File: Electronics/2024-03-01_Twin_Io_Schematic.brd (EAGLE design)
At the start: 160 x 100 mm, 179 parts, among them IC1 7805, IC2 LD1117S33, J1 12402012E212A, U1 INA317IDGKT, U10 INA317IDGKT, U11 INA317IDGKT, U12 INA317IDGKT, U13 ADS131A04IPBSR, U14 ADS131A04IPBSR, U15 ADS131A04IPBSR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

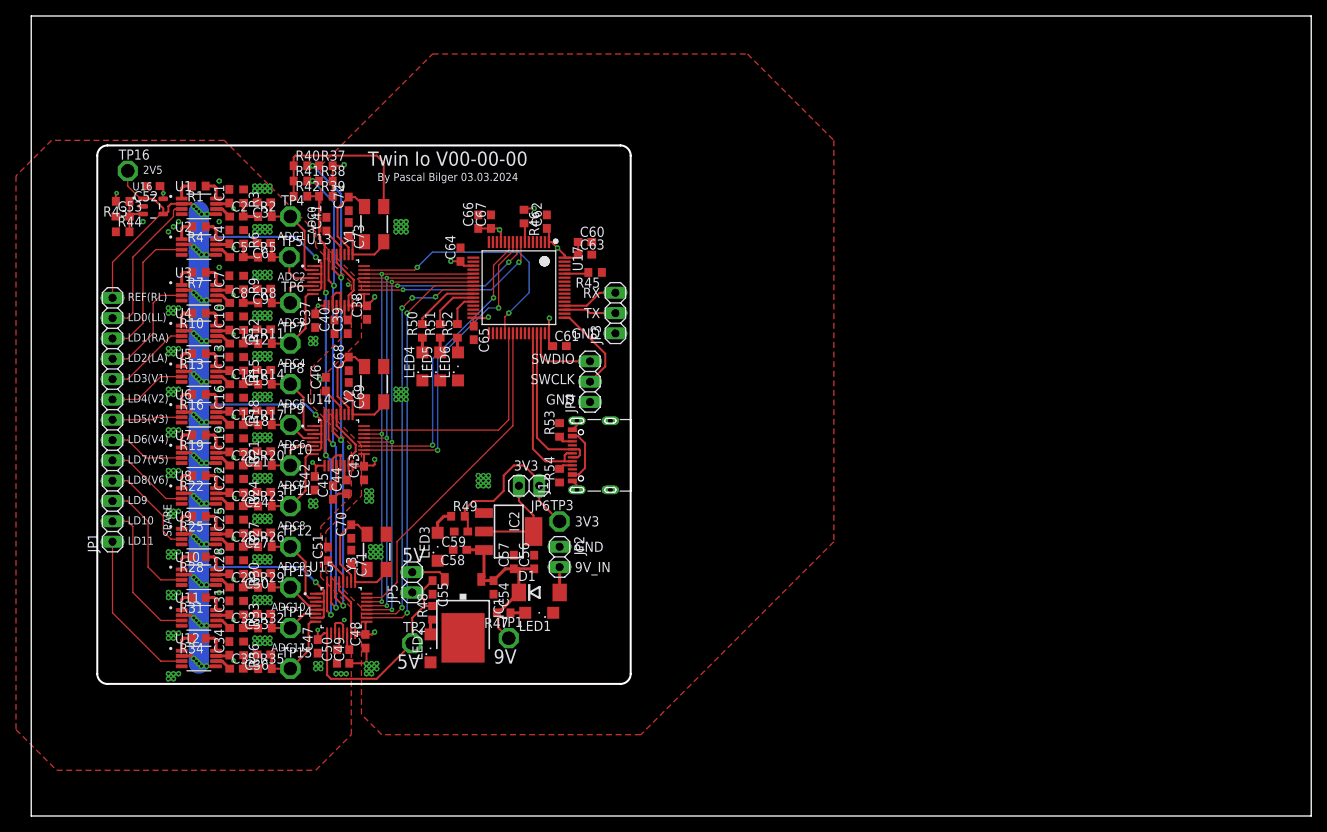
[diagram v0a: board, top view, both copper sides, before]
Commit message: Added possibility for STM32 Timer output to be used for the ADC clock, selectable by 3x 0Ohm resistors
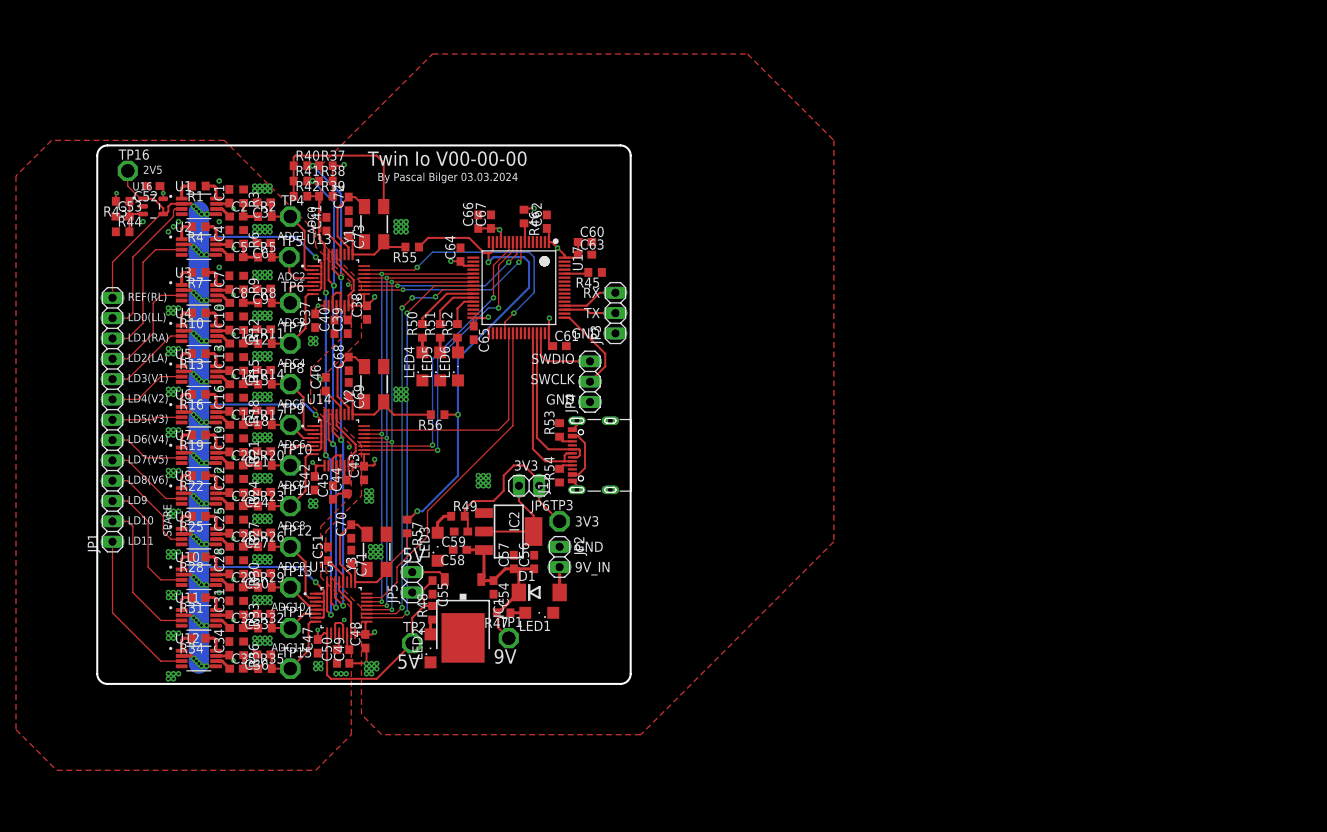
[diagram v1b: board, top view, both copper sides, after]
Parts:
- added R55, R56, R57: 0R, rcl:R0603
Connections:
- new net ADC_CLK: R55.1, R56.1, R57.1, U17.15
- net N$43: now also R56.2
- net N$51: now also R57.2
- net N$8: now also R55.2
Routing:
- net ADC_CLK: track 0.00 -> 59.1 mm, vias 0 -> 3
- net N$43: track 7.30 -> 13.7 mm
- net N$51: track 7.30 -> 12.9 mm
- net N$8: track 7.30 -> 10.3 mm
- net ADC0_CS: track 32.2 -> 33.5 mm
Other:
- board size 160 x 100 mm -> 66.7 x 67.3 mm
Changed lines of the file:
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@@
 <layer number="14" name="Route14" color="22" fill="1" visible="no" active="no"/>
 <layer number="15" name="Route15" color="23" fill="1" visible="no" active="yes"/>
-<layer number="16" name="Bottom" color="1" fill="1" visible="no" active="yes"/>
+<layer number="16" name="Bottom" color="1" fill="1" visible="yes" active="yes"/>
 <layer number="17" name="Pads" color="2" fill="1" visible="yes" active="yes"/>
 <layer number="18" name="Vias" color="2" fill="1" visible="yes" active="yes"/>
@@
 <board>
 <plain>
-<wire x1="0" y1="0" x2="160" y2="0" width="0" layer="20"/>
-<wire x1="160" y1="0" x2="160" y2="100" width="0" layer="20"/>
-<wire x1="160" y1="100" x2="0" y2="100" width="0" layer="20"/>
-<wire x1="0" y1="100" x2="0" y2="0" width="0" layer="20"/>
 <text x="57.785" y="19.05" size="1.778" layer="21">9V</text>
 <text x="45.72" y="18.415" size="1.778" layer="21">5V</text>
@@
 <attribute name="VALUE" x="64.77" y="44.45" size="1.27" layer="27" rot="R180"/>
 </element>
+<element name="R55" library="rcl" library_urn="urn:adsk.eagle:library:334" package="R0603" package3d_urn="urn:adsk.eagle:package:23555/3" value="0R" x="47.625" y="71.12" smashed="yes" rot="R180">
+<attribute name="NAME" x="48.26" y="70.485" size="1.27" layer="25" rot="R180"/>
+<attribute name="POPULARITY" value="70" x="47.625" y="71.12" size="1.778" layer="27" rot="R180" display="off"/>
+<attribute name="SPICEPREFIX" value="R" x="47.625" y="71.12" size="1.778" layer="27" rot="R180" display="off"/>
+<attribute name="VALUE" x="48.26" y="73.025" size="1.27" layer="27" rot="R180"/>
+</element>
+<element name="R56" library="rcl" library_urn="urn:adsk.eagle:library:334" package="R0603" package3d_urn="urn:adsk.eagle:package:23555/3" value="0R" x="50.8" y="50.165" smashed="yes" rot="R180">
+<attribute name="NAME" x="51.435" y="49.53" size="1.27" layer="25" rot="R180"/>
+<attribute name="POPULARITY" value="70" x="50.8" y="50.165" size="1.778" layer="27" rot="R180" display="off"/>
+<attribute name="SPICEPREFIX" value="R" x="50.8" y="50.165" size="1.778" layer="27" rot="R180" display="off"/>
+<attribute name="VALUE" x="51.435" y="52.07" size="1.27" layer="27" rot="R180"/>
+</element>
+<element name="R57" library="rcl" library_urn="urn:adsk.eagle:library:334" package="R0603" package3d_urn="urn:adsk.eagle:package:23555/3" value="0R" x="46.99" y="36.195" smashed="yes" rot="R270">
+<attribute name="NAME" x="47.625" y="36.83" size="1.27" layer="25" rot="R270"/>
+<attribute name="POPULARITY" value="70" x="46.99" y="36.195" size="1.778" layer="27" rot="R270" display="off"/>
+<attribute name="SPICEPREFIX" value="R" x="46.99" y="36.195" size="1.778" layer="27" rot="R270" display="off"/>
+<attribute name="VALUE" x="45.085" y="36.83" size="1.27" layer="27" rot="R270"/>
+</element>
 </elements>
 <signals>
@@
 <vertex x="34.925" y="71.755"/>
 <vertex x="34.925" y="73.66"/>
-<vertex x="25.4" y="83.185"/>
-<vertex x="1.27" y="83.185"/>
+<vertex x="24.13" y="84.455"/>
+<vertex x="2.54" y="84.455"/>
 <vertex x="-1.905" y="80.01"/>
 <vertex x="-1.905" y="10.795"/>
@@
 <wire x1="41.93" y1="27.285" x2="41.95" y2="27.305" width="0.127" layer="1"/>
 <wire x1="43.815" y1="27.305" x2="45.72" y2="29.21" width="0.127" layer="1"/>
-<wire x1="60.21" y1="48.78" x2="60.21" y2="60.34" width="0.127" layer="1"/>
-<wire x1="45.72" y1="29.21" x2="45.72" y2="34.29" width="0.127" layer="1"/>
-<wire x1="45.72" y1="34.29" x2="60.21" y2="48.78" width="0.127" layer="1"/>
 <wire x1="41.95" y1="27.305" x2="43.815" y2="27.305" width="0.127" layer="1"/>
+<wire x1="45.72" y1="29.21" x2="45.72" y2="31.115" width="0.127" layer="1"/>
+<wire x1="45.72" y1="31.115" x2="49.53" y2="34.925" width="0.127" layer="1"/>
+<wire x1="49.53" y1="34.925" x2="49.53" y2="38.1" width="0.127" layer="1"/>
+<wire x1="60.21" y1="48.78" x2="60.21" y2="60.34" width="0.127" layer="1"/>
+<wire x1="49.53" y1="38.1" x2="60.21" y2="48.78" width="0.127" layer="1"/>
 </signal>
 <signal name="ADC2_DRDY">
@@
 <via x="48.26" y="68.58" extent="1-16" drill="0.3048" diameter="0.6096"/>
 <wire x1="48.26" y1="68.58" x2="50.165" y2="70.485" width="0.127" layer="16"/>
-<wire x1="50.165" y1="70.485" x2="60.96" y2="70.485" width="0.127" layer="16"/>
-<wire x1="60.96" y1="70.485" x2="62.23" y2="69.215" width="0.127" layer="16"/>
-<wire x1="62.23" y1="65.405" x2="59.69" y2="62.865" width="0.127" layer="16"/>
-<via x="59.69" y="62.865" extent="1-16" drill="0.3048" diameter="0.6096"/>
-<wire x1="59.69" y1="62.865" x2="59.21" y2="62.385" width="0.127" layer="1"/>
-<wire x1="59.21" y1="62.385" x2="59.21" y2="60.34" width="0.127" layer="1"/>
-<wire x1="62.23" y1="69.215" x2="62.23" y2="65.405" width="0.127" layer="16"/>
+<wire x1="50.165" y1="70.485" x2="62.23" y2="70.485" width="0.127" layer="16"/>
+<wire x1="62.23" y1="70.485" x2="62.865" y2="69.85" width="0.127" layer="16"/>
+<wire x1="62.865" y1="65.405" x2="60.325" y2="62.865" width="0.127" layer="16"/>
+<via x="60.325" y="62.865" extent="1-16" drill="0.3048" diameter="0.6096"/>
+<wire x1="60.325" y1="62.865" x2="59.21" y2="61.75" width="0.127" layer="1"/>
+<wire x1="59.21" y1="61.75" x2="59.21" y2="60.34" width="0.127" layer="1"/>
+<wire x1="62.865" y1="69.85" x2="62.865" y2="65.405" width="0.127" layer="16"/>
 </signal>
 <signal name="USB-">
@@
 <contactref element="U14" pad="25"/>
 <wire x1="40.1675" y1="50.185" x2="42.8825" y2="50.185" width="0.254" layer="1"/>
-<wire x1="44.0625" y1="51.365" x2="44.0625" y2="51.775" width="0.254" layer="1"/>
+<wire x1="44.0625" y1="51.365" x2="44.0625" y2="51.435" width="0.254" layer="1"/>
+<wire x1="44.0625" y1="51.435" x2="44.0625" y2="51.775" width="0.254" layer="1"/>
 <wire x1="42.8825" y1="50.185" x2="44.0625" y2="51.365" width="0.254" layer="1"/>
 <wire x1="39.6875" y1="52.49" x2="40.1675" y2="52.01" width="0.254" layer="1"/>
 <wire x1="40.1675" y1="52.01" x2="40.1675" y2="50.185" width="0.254" layer="1"/>
+<contactref element="R56" pad="2"/>
+<wire x1="49.95" y1="50.165" x2="45.3325" y2="50.165" width="0.254" layer="1"/>
+<wire x1="45.3325" y1="50.165" x2="44.0625" y2="51.435" width="0.254" layer="1"/>
 </signal>
 <signal name="N$48">
@@
 <wire x1="40.005" y1="31.535" x2="40.485" y2="31.055" width="0.254" layer="1"/>
 <wire x1="40.485" y1="31.055" x2="40.485" y2="29.23" width="0.254" layer="1"/>
+<contactref element="R57" pad="2"/>
+<wire x1="44.38" y1="30.82" x2="44.38" y2="31.045" width="0.127" layer="1"/>
+<wire x1="46.99" y1="33.655" x2="46.99" y2="35.345" width="0.127" layer="1"/>
+<wire x1="44.38" y1="31.045" x2="46.99" y2="33.655" width="0.127" layer="1"/>
 </signal>
 <signal name="N$7">
@@
 <wire x1="40.1675" y1="72.0125" x2="40.1675" y2="70.1875" width="0.254" layer="1"/>
 <wire x1="40.1675" y1="70.1875" x2="42.8825" y2="70.1875" width="0.254" layer="1"/>
-<wire x1="44.0625" y1="71.3675" x2="44.0625" y2="71.7775" width="0.254" layer="1"/>
+<wire x1="44.0625" y1="71.3675" x2="44.0625" y2="71.755" width="0.254" layer="1"/>
+<wire x1="44.0625" y1="71.755" x2="44.0625" y2="71.7775" width="0.254" layer="1"/>
 <wire x1="42.8825" y1="70.1875" x2="44.0625" y2="71.3675" width="0.254" layer="1"/>
+<contactref element="R55" pad="2"/>
+<wire x1="46.775" y1="71.12" x2="44.6975" y2="71.12" width="0.254" layer="1"/>
+<wire x1="44.6975" y1="71.12" x2="44.0625" y2="71.755" width="0.254" layer="1"/>
 </signal>
 <signal name="MCO">
@@
 <wire x1="51.054" y1="30.48" x2="51.695" y2="29.839" width="0.254" layer="1"/>
 </signal>
+<signal name="ADC_CLK">
+<contactref element="U17" pad="15"/>
+<contactref element="R55" pad="1"/>
+<contactref element="R56" pad="1"/>
+<contactref element="R57" pad="1"/>
+<wire x1="57.71" y1="71.74" x2="57.71" y2="70.664" width="0.254" layer="1"/>
+<wire x1="57.71" y1="70.664" x2="57.404" y2="70.358" width="0.254" layer="1"/>
+<wire x1="57.404" y1="70.358" x2="57.15" y2="70.358" width="0.254" layer="1"/>
+<wire x1="57.15" y1="70.358" x2="56.642" y2="70.358" width="0.254" layer="1"/>
+<wire x1="49.618" y1="72.263" x2="48.475" y2="71.12" width="0.254" layer="1"/>
+<wire x1="56.642" y1="70.358" x2="54.737" y2="72.263" width="0.254" layer="1"/>
+<wire x1="54.737" y1="72.263" x2="49.618" y2="72.263" width="0.254" layer="1"/>
+<wire x1="57.15" y1="70.358" x2="57.15" y2="69.215" width="0.254" layer="1"/>
+<via x="57.15" y="69.215" extent="1-16" drill="0.35"/>
+<wire x1="57.15" y1="69.215" x2="57.785" y2="69.85" width="0.254" layer="16"/>
+<wire x1="61.595" y1="69.85" x2="62.23" y2="69.215" width="0.254" layer="16"/>
+<wire x1="62.23" y1="69.215" x2="62.23" y2="66.04" width="0.254" layer="16"/>
+<wire x1="53.34" y1="57.15" x2="53.34" y2="50.165" width="0.254" layer="16"/>
+<via x="53.34" y="50.165" extent="1-16" drill="0.35"/>
+<wire x1="53.34" y1="50.165" x2="51.65" y2="50.165" width="0.254" layer="1"/>
+<wire x1="57.785" y1="69.85" x2="61.595" y2="69.85" width="0.254" layer="16"/>
+<wire x1="62.23" y1="66.04" x2="53.34" y2="57.15" width="0.254" layer="16"/>
+<wire x1="53.34" y1="50.165" x2="53.34" y2="42.545" width="0.254" layer="16"/>
+<wire x1="53.34" y1="42.545" x2="48.895" y2="38.1" width="0.254" layer="16"/>
+<wire x1="48.895" y1="38.1" x2="48.26" y2="38.1" width="0.254" layer="16"/>
+<via x="48.26" y="38.1" extent="1-16" drill="0.35"/>
+<wire x1="48.26" y1="38.1" x2="47.205" y2="37.045" width="0.254" layer="1"/>
+<wire x1="47.205" y1="37.045" x2="46.99" y2="37.045" width="0.254" layer="1"/>
+</signal>
 </signals>
